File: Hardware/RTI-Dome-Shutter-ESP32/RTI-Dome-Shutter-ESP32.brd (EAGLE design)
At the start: 111.1 x 76.3 mm, 100 parts, among them IC1 REG1117FA-5.0_500, IC2 24LC64T-I/SN, IC8 REG1117-3.3V, J2 XT60PW-M, T1 MMBT3904LT1, T2 MMBT3904LT1, T3 MMBT3904LT1, U1 W5500, U2 ESP32-DevKitC ESP32-WROOM-32U, X9 J1011F01PNL

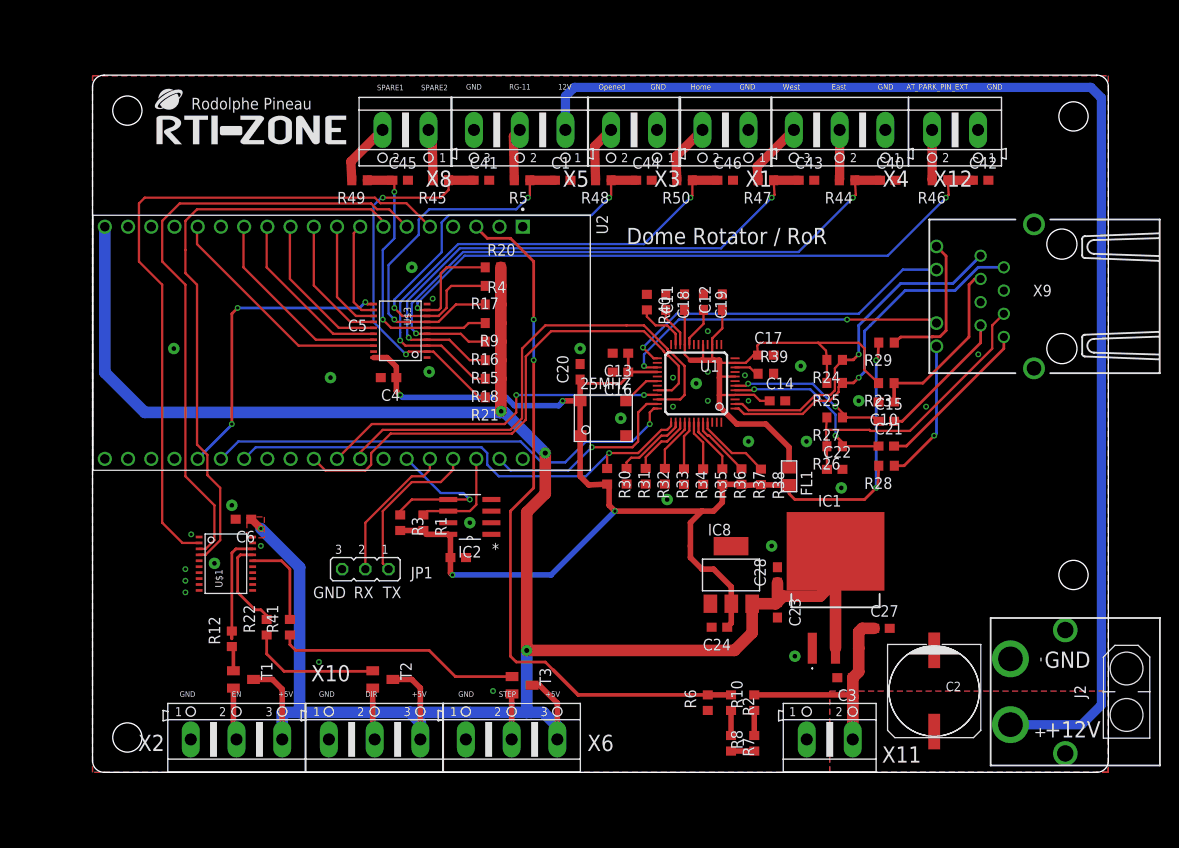
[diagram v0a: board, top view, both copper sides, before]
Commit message: Adding ESP32 version of the shutter controller
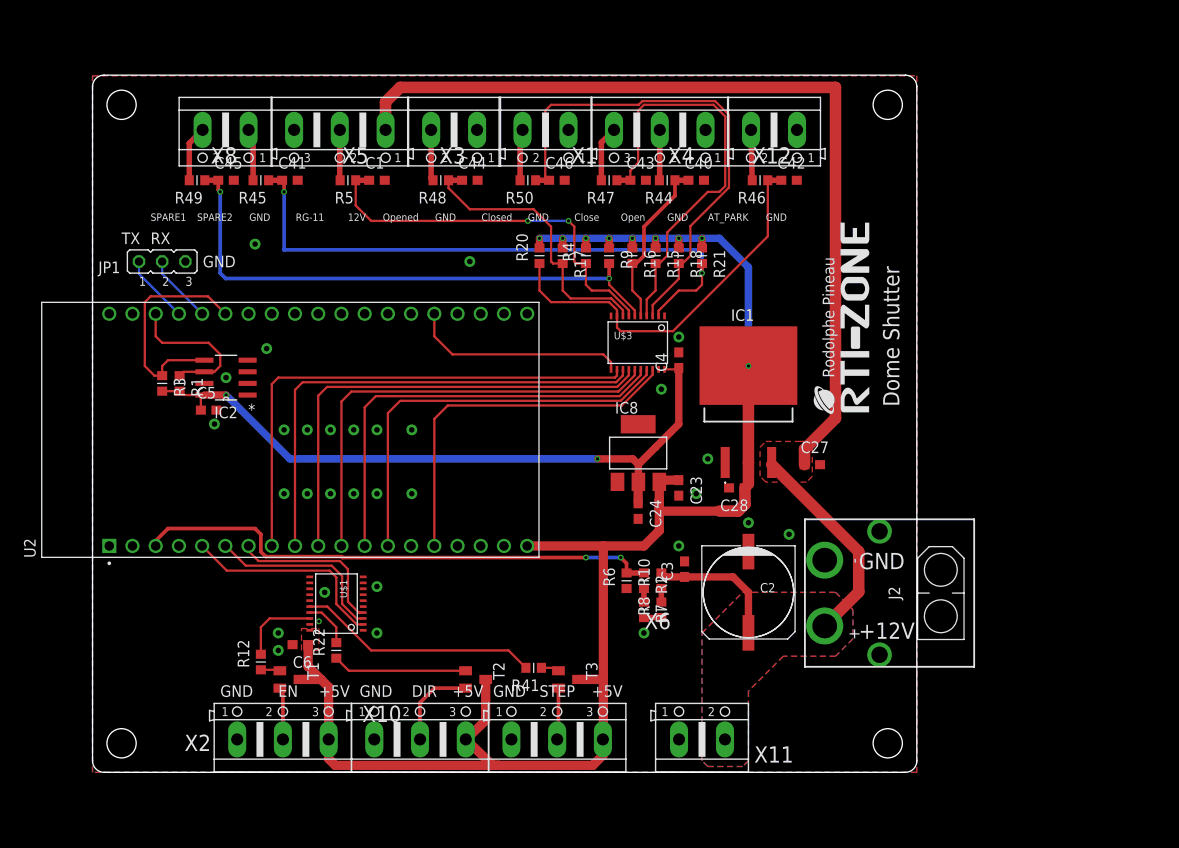
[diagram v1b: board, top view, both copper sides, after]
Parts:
- removed 25MHZ: CB3LV-OSCILATOR, rti:SMD-7050_4P
- removed C10: 22nF, rcl:C0603
- removed C11, C12, C14, C16, C17, C20: 100nF, rcl:C0603
- removed C13, C18, C22: 10nF, rcl:C0603
- removed C15, C21: 6.8nF, rcl:C0603
- removed C19: 4.7uF, rcl:C0603
- removed FL1: BLM21AG121SN1D, BLM21AG121SN1D:L0805
- removed R23: 10 1%, rcl:R0603
- removed R24, R25, R26, R27: 49.9 1%, rcl:R0603
- removed R28, R29: 330, rcl:R0603
- removed R30, R31, R32, R33, R34, R35, R36, R37, R38, R40: 4.7K, rcl:R0603
- removed R39: 12.4K 1%, rcl:R0603
- removed U1: W5500, W5500:LQFP48
- removed X9: J1011F01PNL, rti:J1011F01PNL
- C1, C23, C24, C27, C28, C3, C4, C40, C41, C42, C43, C44, C45, C46, C5, C6: device rcl:C0603 -> rti:C0603
- IC2: device Microchip_By_element14_Batch_1:SOIC127P600X175-8N -> rti:SOIC127P600X175-8N
- R1, R10, R12, R15, R16, R17, R18, R2, R20, R21, R22, R3, R4, R41, R44, R45, R46, R47, R48, R49, R5, R50, R6, R7, R8, R9: device rcl:R0603 -> rti:R0603
- T1, T2, T3: value MMBT3904LT1 -> (none); device samacsys:SOT23 -> transistor:SOT23-BEC
- U2: value ESP32-DevKitC ESP32-WROOM-32U -> ESP32-DevKitC ESP32-WROOM-32D
- moved U$4 83.3 mm to (85.0, 39.4), turned to 90 degrees
- moved JP1 40.3 mm to (7.62, 55.9), turned to 0 degrees
- moved C4 31.8 mm to (64.1, 45.1), turned to 90 degrees
- moved C5 31.7 mm to (12.7, 39.6)
- moved R1 30.7 mm to (9.53, 42.5)
- moved IC2 30.7 mm to (14.6, 43.2)
- moved R3 30.2 mm to (7.62, 42.5)
- moved R21 27.6 mm to (66.7, 56.5), turned to 270 degrees
- moved R41 27.0 mm to (48.3, 11.4), turned to 180 degrees
- moved U$3 26.1 mm to (59.7, 47.0), turned to 270 degrees
- moved R18 24.4 mm to (64.1, 56.5), turned to 270 degrees
- moved J2 23.0 mm to (80.1, 19.6)
- moved C2 23.0 mm to (71.8, 19.7)
- moved IC1 22.4 mm to (71.8, 40.6)
- moved C3 21.2 mm to (64.8, 22.2), turned to 90 degrees
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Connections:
- removed net ACT_LED: U1.27, X9.11
- removed net AVDD: C11.1, C12.1, C14.1, C17.1, FL1.1, R23.2, R24.2, R25.2, U1.11, U1.15, U1.17, U1.21, U1.4, U1.8
- removed net LINK_ACK: U1.25, X9.10
- removed net N$10: R28.1, X9.12
- removed net N$11: C15.2, X9.7
- removed net N$12: C21.2, X9.8
- removed net N$13: C10.1, R23.1, X9.3
- removed net N$17: U1.26
- removed net N$22: R31.1, U1.38
- removed net N$23: R32.1, U1.39
- removed net N$24: R33.1, U1.40
- removed net N$25: R34.1, U1.41
- removed net N$26: R35.1, U1.42
- removed net N$27: R36.1, U1.43
- removed net N$28: R37.1, U1.44
- removed net N$29: R38.1, U1.45
- removed net N$31: C19.2, U1.20
- removed net N$32: U1.18
- removed net N$33: C18.2, U1.22
- removed net N$34: R39.1, U1.10
- removed net N$35: R40.2, U1.23
- removed net N$7: C22.1, R26.2, R27.2, X9.6
- removed net N$8: R29.1, X9.9
- removed net RXN: C21.1, R26.1, U1.5
- removed net RXP: C15.1, R27.1, U1.6
- removed net TXN: R25.1, U1.1, X9.2
- removed net TXP: R24.1, U1.2, X9.1
- removed net XI: 25MHZ.3, U1.30
- removed net XO: U1.31
- net 3.3V: no longer 25MHZ.1, 25MHZ.4, C13.1, C16.1, C20.1, FL1.2, R28.2, R29.2, R30.2, R36.2, R37.2, R38.2, U1.28
- net DIR-5V_TR: now also T2.B; no longer T2.1
- net DIR_5V_OUT: now also T2.E; no longer T2.2
- net EN-5V_TR: now also T1.B; no longer T1.1
- net EN_5V_OUT: now also T1.E; no longer T1.2
- net ETH_CS: no longer U1.32
- net ETH_RESET: no longer R30.1, U1.37
- net GND: no longer 25MHZ.2, C10.2, C11.2, C12.2, C13.2, C14.2, C16.2, C17.2, C18.1, C19.1, C20.2, C22.2, R31.2, R32.2, R33.2, R34.2, R35.2, R39.2, R40.1, U1.14, U1.16, U1.19, U1.29, U1.3, U1.48, U1.9, X9.4, X9.5, X9.M1, X9.M2
- net INT_N: no longer U1.36
- net SCLK: no longer U1.33
- net SDI: no longer U1.34
- net SDO: no longer U1.35
- net STEP-5V_TR: now also T3.B; no longer T3.1
- net STEP_5V_OUT: now also T3.E; no longer T3.2
- net VCC: now also T1.C, T2.C, T3.C; no longer T1.3, T2.3, T3.3
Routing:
- net VCC: track 255.2 -> 176.7 mm, vias 4 -> 9
- net 3.3V: track 153.5 -> 75.5 mm, vias 6 -> 2
- net AVDD: track 68.1 -> 0.00 mm
- net ETH_CS: track 57.7 -> 0.00 mm
- net SDI: track 54.7 -> 0.00 mm
- net ETH_RESET: track 53.8 -> 0.00 mm, vias 1 -> 0
- net INT_N: track 52.7 -> 0.00 mm, vias 1 -> 0
- net M_EN: track 74.3 -> 22.9 mm
- net BUTTON_EAST_OPEN_5V: track 69.3 -> 18.9 mm, vias 2 -> 0
- net M_DIR: track 67.9 -> 20.2 mm
- net SHUTTER_OPENED: track 11.1 -> 56.5 mm
- net M_STEP: track 63.1 -> 18.0 mm
- net RG-11: track 12.6 -> 54.3 mm
- net TXN: track 39.3 -> 0.00 mm, vias 1 -> 0
- net SCLK: track 39.1 -> 0.00 mm, vias 2 -> 0
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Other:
- board size 111.1 x 76.3 mm -> 90.2 x 76.3 mm
- board text added: "AT_PARK"
- board text added: "Close"
- board text added: "Closed"
- board text added: "Dome Shutter"
- board text added: "Open"
- board text removed: "AT_PARK_PIN_EXT"
- board text removed: "Dome Rotator / RoR"
- board text removed: "East"
- board text removed: "Home"
- board text removed: "West"

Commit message: Fixed a lot of issue with the ESP32 and serial ports.
Alpaca Discovery and API server are now running in their own tasks.
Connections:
- removed net N$15: U2.23
- net AT_PARK_PIN: now also U2.6; no longer U2.24
- net HOME_SHUTTER_CLOSED: now also U2.23; no longer U2.13
- net M_DIR: now also U2.24; no longer U2.6
- net M_EN: now also U2.15; no longer U2.5
- net RX2: now also JP1.2
- net RXD0: no longer JP1.2
- net SPARE1: now also U2.5; no longer U2.15
- net TX2: now also JP1.1
- net TXD0: no longer JP1.1
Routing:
- net HOME_SHUTTER_CLOSED: track 45.2 -> 0.00 mm
- net SPARE1: track 40.4 -> 0.00 mm
- net RX2: track 0.00 -> 25.7 mm
- net TX2: track 0.00 -> 24.9 mm
- net AT_PARK_PIN: track 23.8 -> 0.00 mm
- net M_EN: track 22.9 -> 0.00 mm
- net M_DIR: track 20.2 -> 0.00 mm
- net RXD0: track 7.53 -> 0.00 mm
- net TXD0: track 7.53 -> 0.00 mm

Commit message: Latest board fixes with the extra output for lower shutter/other things.
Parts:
- removed U2: ESP32-DevKitC ESP32-WROOM-32D, ESP32-DEVKITC-32D:MODULE_ESP32-DEVKITC-32D
- added U1: ESP32-DevKitC ESP32-WROOM-32U, ESP32-DEVKITC-32D:MODULE_ESP32-DEVKITC-32D
- added X7: (no value), rti:AK500/3
- moved JP1 22.2 mm to (29.8, 55.2)
- moved X11 8.26 mm to (74.9, 3.60)
- moved X6 5.08 mm to (45.7, 3.60)
- moved X10 5.08 mm to (30.7, 3.60)
- moved X2 5.08 mm to (15.7, 3.60)
- moved R22 0.64 mm to (26.0, 13.3)
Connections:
- removed net INT_N: U2.25
- removed net N$20: U2.1
- removed net N$21: U2.2
- removed net N$36: U2.4
- new net N$10: U1.2
- new net N$11: U1.4
- new net N$6: U$1.P$13
- new net N$7: U$1.P$12
- new net N$8: U$1.P$11
- new net N$9: U1.1
- new net SPARE_OUT1: U$1.P$5, U1.25
- new net SPARE_OUT1_5V: U$1.P$15, X7.3
- new net SPARE_OUT2: U$1.P$6, U1.13
- new net SPARE_OUT2_5V: U$1.P$14, X7.2
- net AT_PARK_PIN: now also U1.6; no longer U2.6
- net BUTTON_EAST_OPEN: now also U1.11; no longer U2.11
- net BUTTON_WEST_CLOSE: now also U1.12; no longer U2.12
- net ETH_CS: now also U1.29; no longer U2.29
- net ETH_RESET: now also U1.26; no longer U2.26
- net GND: now also U1.14, U1.32, U1.38, X7.1; no longer U$1.P$5, U$1.P$6, U2.14, U2.32, U2.38
- net HOME_SHUTTER_CLOSED: now also U1.23; no longer U2.23
- net M_DIR: now also U1.24; no longer U2.24
- net M_EN: now also U1.15; no longer U2.15
- net M_STEP: now also U1.7; no longer U2.7
- net RG-11: now also U1.9; no longer U2.9
- net RX2: now also U1.27; no longer U2.27
- net RXD0: now also U1.34; no longer U2.34
- net SCL: now also U1.36; no longer U2.36
- net SCLK: now also U1.30; no longer U2.30
- net SDA: now also U1.33; no longer U2.33
- net SDI: now also U1.31; no longer U2.31
- net SDO: now also U1.37; no longer U2.37
- net SHUTTER_OPENED: now also U1.8; no longer U2.8
- net SPARE1: now also U1.5; no longer U2.5
- net SPARE2: now also U1.10; no longer U2.10
- net TX2: now also U1.28; no longer U2.28
- net TXD0: now also U1.35; no longer U2.35
- net VCC: now also U1.19; no longer U2.19
- net VPIN: now also U1.3; no longer U2.3
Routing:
- net SPARE1: track 0.00 -> 66.1 mm
- net AT_PARK_PIN: track 0.00 -> 56.8 mm
- net SPARE_OUT1_5V: track 0.00 -> 50.6 mm, vias 0 -> 2
- net SPARE_OUT2_5V: track 0.00 -> 48.1 mm, vias 0 -> 2
- net M_DIR: track 0.00 -> 38.8 mm, vias 0 -> 4
- net SPARE_OUT1: track 0.00 -> 35.7 mm, vias 0 -> 4
- net HOME_SHUTTER_CLOSED: track 0.00 -> 25.0 mm
- net RX2: track 25.7 -> 5.08 mm
- net TX2: track 24.9 -> 5.08 mm
- net M_EN: track 0.00 -> 14.8 mm, vias 0 -> 1
- net SPARE_OUT2: track 0.00 -> 8.16 mm, vias 0 -> 1
- net DIR_5V_OUT: track 9.68 -> 14.6 mm
- net STEP_5V_OUT: track 5.67 -> 10.0 mm
- net SPARE2_IN_5V: track 61.5 -> 65.1 mm
- net EN_5V_OUT: track 5.75 -> 9.27 mm
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
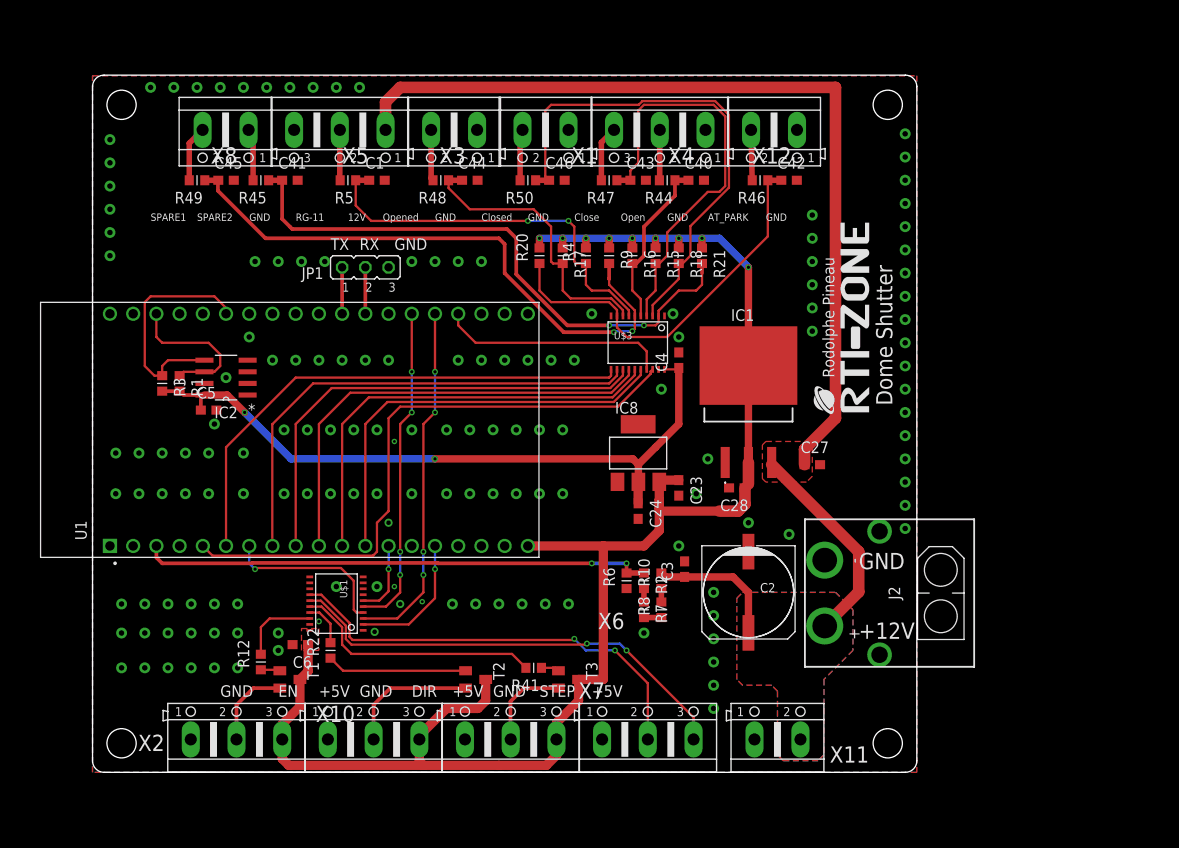
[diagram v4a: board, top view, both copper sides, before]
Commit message: Now using Wurth connector for rotator and shutter.
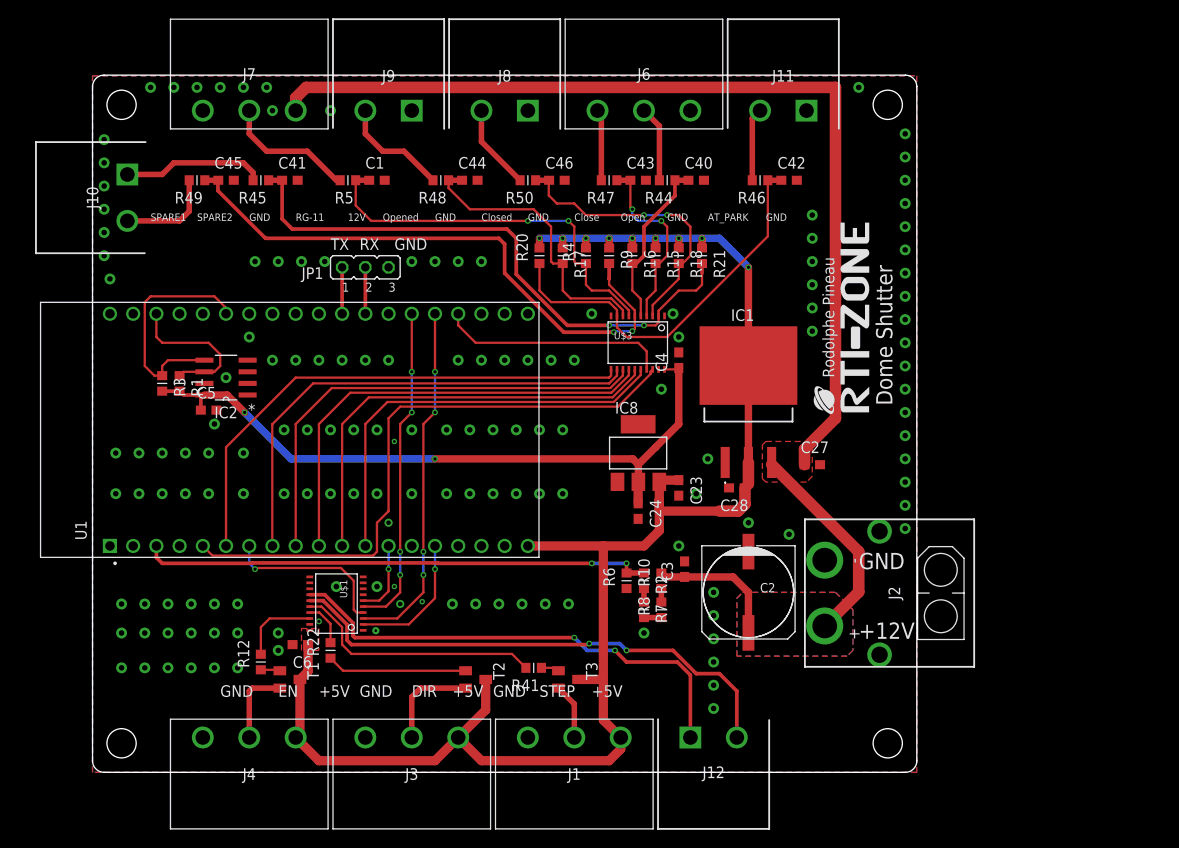
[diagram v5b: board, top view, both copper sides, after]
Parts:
- removed X1, X11, X12, X3, X8: (no value), rti:AK500/2
- removed X10, X2, X4, X5, X6, X7: (no value), rti:AK500/3
- added J1, J3, J4, J6, J7: 691313510003, samacsys:691313510003
- added J10, J11, J12, J8, J9: 691313510002, samacsys:SHDRRA2W100P0X508_1X2_1216X120
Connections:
- net +12V: now also J7.1; no longer X11.2, X5.1
- net AT_PARK_PIN-IN_EXT: now also J11.2; no longer X12.2
- net BUTTON_EAST_OPEN-IN_EXT: now also J6.2; no longer X4.2
- net BUTTON_WEST_CLOSE-IN_EXT: now also J6.3; no longer X4.3
- net DIR_5V_OUT: now also J3.2; no longer X10.2
- net EN_5V_OUT: now also J4.2; no longer X2.2
- net GND: now also J1.1, J11.1, J3.1, J4.1, J6.1, J7.3, J8.1, J9.1; no longer X1.1, X10.1, X11.1, X12.1, X2.1, X3.1, X4.1, X5.3, X6.1, X7.1
- net HOME_SHUTTER_CLOSED-IN_EXT: now also J8.2; no longer X1.2
- net RG-11-IN_EXT: now also J7.2; no longer X5.2
- net SHUTTER_OPENED-IN_EXT: now also J9.2; no longer X3.2
- net SPARE1-IN_EXT: now also J10.1; no longer X8.1
- net SPARE2-IN_EXT: now also J10.2; no longer X8.2
- net SPARE_OUT1_5V: now also J12.2; no longer X7.3
- net SPARE_OUT2_5V: now also J12.1; no longer X7.2
- net STEP_5V_OUT: now also J1.2; no longer X6.2
- net VCC: now also J1.3, J3.3, J4.3; no longer X10.3, X2.3, X6.3
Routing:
- net BUTTON_WEST_CLOSE_IN_5V: track 46.1 -> 20.6 mm, vias 0 -> 2
- net HOME_SHUTTER_CLOSED_IN_5V: track 56.1 -> 32.2 mm, vias 0 -> 2
- net SPARE1-IN_EXT: track 5.72 -> 15.6 mm
- net RG-11-IN_EXT: track 5.53 -> 14.6 mm
- net +12V: track 133.6 -> 141.6 mm
- net SHUTTER_OPENED-IN_EXT: track 5.60 -> 12.0 mm
- net SPARE_OUT1_5V: track 50.6 -> 57.0 mm
- net SPARE_OUT2_5V: track 48.1 -> 52.9 mm
- net SPARE2-IN_EXT: track 6.11 -> 10.6 mm
- net STEP_5V_OUT: track 10.0 -> 6.12 mm
- net DIR_5V_OUT: track 14.6 -> 10.7 mm
- net HOME_SHUTTER_CLOSED-IN_EXT: track 5.62 -> 9.37 mm
- net BUTTON_EAST_OPEN-IN_EXT: track 5.52 -> 8.32 mm
- net VCC: track 177.9 -> 175.4 mm
- net AT_PARK_PIN-IN_EXT: track 5.52 -> 7.97 mm
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
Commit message: Fix components orientation in the library to match JLCPCB
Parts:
- U1: value ESP32-DevKitC ESP32-WROOM-32U -> ESP32-DEVKITC-32E
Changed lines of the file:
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@@
 <attribute name="VALUE" x="26.289" y="50.927" size="1.27" layer="27" ratio="10"/>
 </element>
-<element name="U1" library="ESP32-DEVKITC-32D" library_urn="urn:adsk.eagle:library:44270575" package="MODULE_ESP32-DEVKITC-32D" package3d_urn="urn:adsk.eagle:package:44270578/5" value="ESP32-DevKitC ESP32-WROOM-32U" x="22.225" y="37.465" smashed="yes" rot="R90">
+<element name="U1" library="ESP32-DEVKITC-32D" library_urn="urn:adsk.eagle:library:44270575" package="MODULE_ESP32-DEVKITC-32D" package3d_urn="urn:adsk.eagle:package:44270578/5" value="ESP32-DEVKITC-32E" x="22.225" y="37.465" smashed="yes" rot="R90">
 <attribute name="AVAILABILITY" value="In Stock" x="22.225" y="37.465" size="1.778" layer="27" rot="R90" display="off"/>
 <attribute name="CHECK_PRICES" value="https://www.snapeda.com/parts/ESP32-DEVKITC-32D/Espressif+Systems/view-part/?ref=eda" x="22.225" y="37.465" size="1.778" layer="27" rot="R90" display="off"/>
-<attribute name="DESCRIPTION" value="
-WiFi Development Tools (802.11) ESP32 General Development Kit, ESP32-WROOM-32D on the board
-" x="22.225" y="37.465" size="1.778" layer="27" rot="R90" display="off"/>
+<attribute name="DESCRIPTION" value=" WiFi Development Tools (802.11) ESP32 General Development Kit, ESP32-WROOM-32D on the board " x="22.225" y="37.465" size="1.778" layer="27" rot="R90" display="off"/>
 <attribute name="MF" value="Espressif Systems" x="22.225" y="37.465" size="1.778" layer="27" rot="R90" display="off"/>
 <attribute name="MP" value="ESP32-DEVKITC-32D" x="22.225" y="37.465" size="1.778" layer="27" rot="R90" display="off"/>
